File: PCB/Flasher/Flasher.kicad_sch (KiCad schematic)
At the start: 62 parts, among them J1 Reset, J2 RJ12, J3 USB, J4 USB-C-Socket-V, J5 TF_PUSH, SW1 SW_Push_DPDT, U1 ESP32-S3-MINI-1, U2 TPS562246, U3 FT231XQ, U4 TPS22916CNYFPR, U5 TPS22916CNYFPR

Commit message: LED update
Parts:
- added D15, D16, D17, D18, D19, D20, D22, D24, D25, D26, D27, D28, D29: XL-1010RGBC-WS2812B, RevK:SMD1615, symbol RevK:WS2812B-1.5mm
- D1, D10, D11, D2, D3, D4, D5, D6, D7, D8, D9: footprint RevK:SMD1010 -> RevK:SMD1615; symbol RevK:WS2812B-1mm -> RevK:WS2812B-1.5mm; MPN C5349953 -> C5349954
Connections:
- net +3.3V: now also D1.3 (+), D10.3 (+), D11.3 (+), D2.3 (+), D3.3 (+), D4.3 (+), D5.3 (+), D6.3 (+), D7.3 (+), D8.3 (+), D9.3 (+), D15.3 (+), D16.3 (+), D17.3 (+), D18.3 (+), D19.3 (+), D20.3 (+), D22.3 (+), D24.3 (+), D25.3 (+), D26.3 (+), D27.3 (+), D28.3 (+), D29.3 (+); no longer D1.2 (+), D10.2 (+), D11.2 (+), D2.2 (+), D3.2 (+), D4.2 (+), D5.2 (+), D6.2 (+), D7.2 (+), D8.2 (+), D9.2 (+)
- net GND: now also D1.1 (-), D10.1 (-), D11.1 (-), D2.1 (-), D3.1 (-), D4.1 (-), D5.1 (-), D6.1 (-), D7.1 (-), D8.1 (-), D9.1 (-), D15.1 (-), D16.1 (-), D17.1 (-), D18.1 (-), D19.1 (-), D20.1 (-), D22.1 (-), D24.1 (-), D25.1 (-), D26.1 (-), D27.1 (-), D28.1 (-), D29.1 (-); no longer D1.3 (-), D10.3 (-), D11.3 (-), D2.3 (-), D3.3 (-), D4.3 (-), D5.3 (-), D6.3 (-), D7.3 (-), D8.3 (-), D9.3 (-)
- net LED: now also D1.2 (I); no longer D1.4 (I)
- net at D6.4 (O): now also D7.2 (I); no longer D5.1 (O)
- net at D5.4 (O): now also D6.2 (I); no longer D4.1 (O)
- net at D7.4 (O): now also D8.2 (I); no longer D6.1 (O)
- net at D11.4 (O): now also D15.2 (I); no longer D10.1 (O)
- net at D10.4 (O): now also D11.2 (I); no longer D9.1 (O)
- net at D3.4 (O): now also D4.2 (I); no longer D2.1 (O)
- net at D2.4 (O): now also D3.2 (I); no longer D1.1 (O)
- net at D8.4 (O): now also D9.2 (I); no longer D7.1 (O)
- net at D4.4 (O): now also D5.2 (I); no longer D3.1 (O)
- net at D9.4 (O): now also D10.2 (I); no longer D8.1 (O)
- new net: D27.4 (O), D28.2 (I)
- new net: D28.4 (O), D29.2 (I)
- new net: D16.4 (O), D17.2 (I)
- new net: D17.4 (O), D18.2 (I)
- new net: D1.4 (O), D2.2 (I)
- new net: D22.4 (O), D24.2 (I)
- new net: D24.4 (O), D25.2 (I)
- new net: D26.4 (O), D27.2 (I)
- new net: D25.4 (O), D26.2 (I)
- new net: D19.4 (O), D20.2 (I)
- new net: D20.4 (O), D22.2 (I)
- new net: D15.4 (O), D16.2 (I)
- new net: D18.4 (O), D19.2 (I)
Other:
- moved on the sheet: C14, C15, C16, D1, D10, D11, D2, D3, D4, D5, D6, D7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

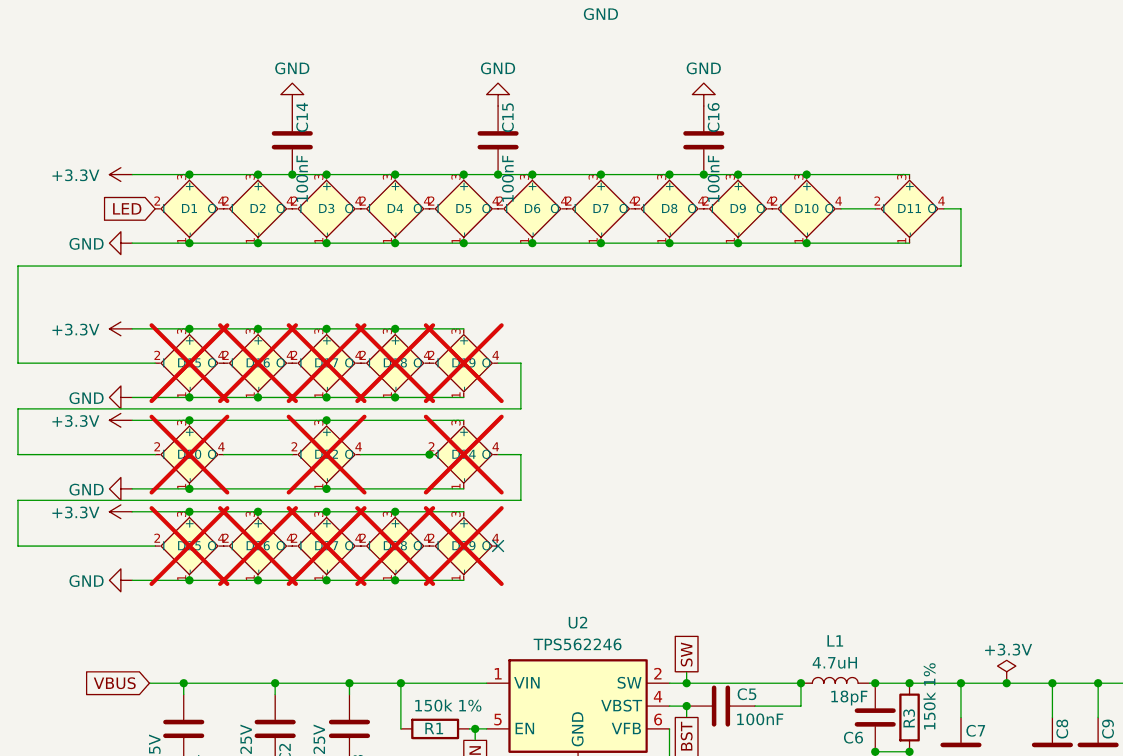
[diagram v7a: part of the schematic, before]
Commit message: New LED
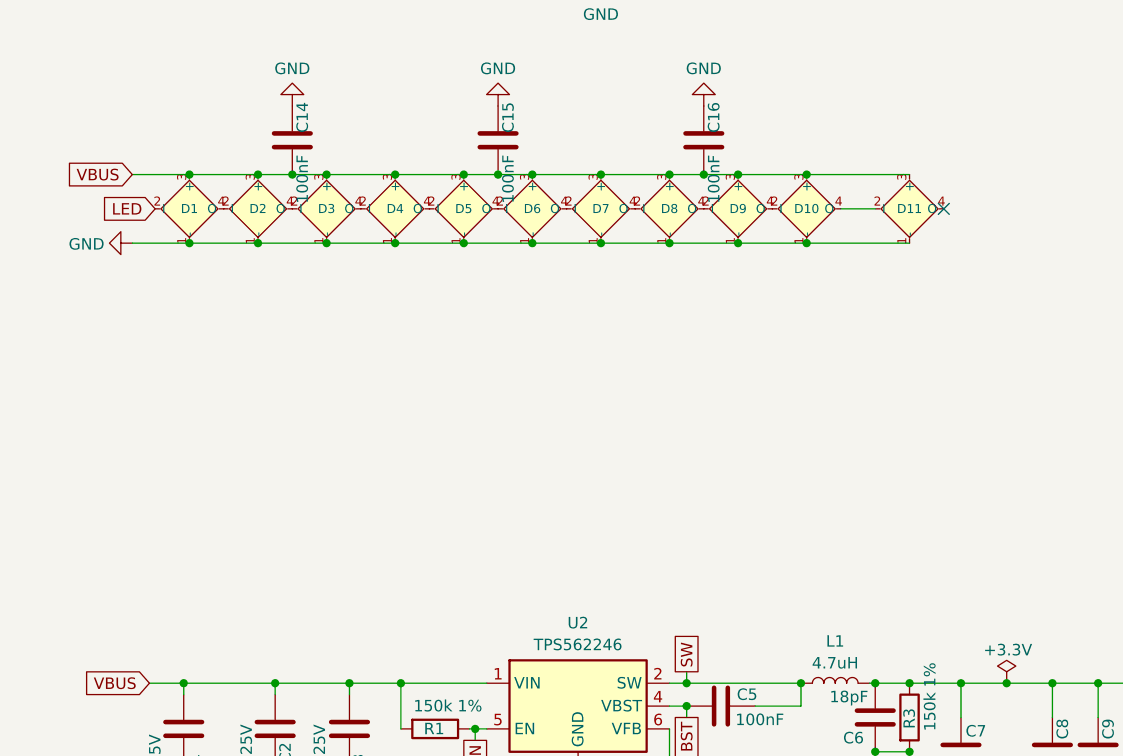
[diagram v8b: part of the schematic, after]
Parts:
- removed D15, D16, D17, D18, D19, D20, D22, D24, D25, D26, D27, D28, D29: XL-1010RGBC-WS2812B, RevK:SMD1615, symbol RevK:WS2812B-1.5mm
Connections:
- net +3.3V: no longer C14.1, C15.1, C16.1, D1.3 (+), D10.3 (+), D11.3 (+), D2.3 (+), D3.3 (+), D4.3 (+), D5.3 (+), D6.3 (+), D7.3 (+), D8.3 (+), D9.3 (+)
- net VBUS: now also C14.1, C15.1, C16.1, D1.3 (+), D10.3 (+), D11.3 (+), D2.3 (+), D3.3 (+), D4.3 (+), D5.3 (+), D6.3 (+), D7.3 (+), D8.3 (+), D9.3 (+)
